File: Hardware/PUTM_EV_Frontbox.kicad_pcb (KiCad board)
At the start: 4 copper layers, 97 x 70 mm, 188 parts, among them IC1 TPS54202HDDCR, J1 XIAO ESP32S3 Sense, J2 Conn_02x16_Counter_Clockwise, J3 FTSH-107-01-L-D-K, Q1 SI2347DS-T1-GE3, U1 TLV743P, U10 MCP6N11-001E/SN, U11 MCP6002-xSN, U12 TLP291-4, U13 TLP291-4, U14 FODM217B, U2 TLV743P, U3 TLV743P, U4 TLV743P, U5 LM4040C33FTA, U6 STM32G484RETx, U7 ADM3057ExRW, U8 ADM3057ExRW, U9 MCP6N11-001E/SN, Y1 ATX-11-F-32.000MHZ-F05-T

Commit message: Sync
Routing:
- net /Connector/DRIVER_KILL: track 103.8 -> 105.6 mm
- net GND: vias 178 -> 183
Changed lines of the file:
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@@
 	)
 	(via
+		(at 144.8 111.4)
+		(size 0.56)
+		(drill 0.3)
+		(layers "F.Cu" "B.Cu")
+		(free yes)
+		(net 2)
+	)
+	(via
 		(at 67.2 99.4)
 		(size 0.56)
@@
 	)
 	(via
+		(at 144.8 112.2)
+		(size 0.56)
+		(drill 0.3)
+		(layers "F.Cu" "B.Cu")
+		(free yes)
+		(net 2)
+	)
+	(via
 		(at 140.5 146)
 		(size 0.56)
@@
 	)
 	(via
+		(at 144 112.2)
+		(size 0.56)
+		(drill 0.3)
+		(layers "F.Cu" "B.Cu")
+		(free yes)
+		(net 2)
+	)
+	(via
 		(at 131 146)
 		(size 0.56)
@@
 	)
 	(via
+		(at 143 111.6)
+		(size 0.56)
+		(drill 0.3)
+		(layers "F.Cu" "B.Cu")
+		(free yes)
+		(net 2)
+	)
+	(via
 		(at 99.2 108.6)
 		(size 0.56)
@@
 	)
 	(via
+		(at 144 111.4)
+		(size 0.56)
+		(drill 0.3)
+		(layers "F.Cu" "B.Cu")
+		(free yes)
+		(net 2)
+	)
+	(via
 		(at 128.5 146)
 		(size 0.56)
@@
 	)
 	(via
-		(at 110.683652 106.613332)
+		(at 111.98 107.06)
 		(size 0.56)
 		(drill 0.3)
@@
 	)
 	(segment
-		(start 110.683652 106.613332)
-		(end 111.13032 107.06)
+		(start 111.98 107.06)
+		(end 133.35 107.06)
 		(width 0.4)
 		(layer "B.Cu")
@@
 	)
 	(segment
-		(start 111.13032 107.06)
-		(end 133.35 107.06)
+		(start 104.338232 92.351)
+		(end 111.261768 92.351)
 		(width 0.4)
-		(layer "B.Cu")
+		(layer "In2.Cu")
 		(net 83)
 	)
 	(segment
-		(start 114.82 89.77)
-		(end 112.239 92.351)
+		(start 99.973 96.716232)
+		(end 99.973 96.413464)
 		(width 0.4)
 		(layer "In2.Cu")
@@
 	)
 	(segment
-		(start 103.579 92.351)
-		(end 99.973 95.957)
+		(start 102.987696 108.38)
+		(end 99.973 105.365304)
 		(width 0.4)
 		(layer "In2.Cu")
@@
 	)
 	(segment
-		(start 114.82 88.3)
-		(end 114.82 89.77)
+		(start 100.295768 95.634232)
+		(end 103.256232 92.673768)
+		(width 0.4)
+		(layer "In2.Cu")
+		(net 83)
+	)
+	(segment
+		(start 104.035464 92.351)
+		(end 104.338232 92.351)
+		(width 0.4)
+		(layer "In2.Cu")
+		(net 83)
+	)
+	(segment
+		(start 99.973 95.957)
+		(end 100.295768 95.634232)
+		(width 0.4)
+		(layer "In2.Cu")
+		(net 83)
+	)
+	(segment
+		(start 103.256232 92.673768)
+		(end 103.579 92.351)
 		(width 0.4)
 		(layer "In2.Cu")
@@
 	(segment
 		(start 115.32 87.8)
-		(end 114.82 88.3)
+		(end 119.96 87.8)
 		(width 0.4)
 		(layer "In2.Cu")
@@
 	)
 	(segment
-		(start 99.973 95.957)
-		(end 99.973 104.253)
+		(start 103.881768 92.351)
+		(end 104.035464 92.351)
 		(width 0.4)
 		(layer "In2.Cu")
@@
 	)
 	(segment
-		(start 99.973 104.253)
-		(end 102.333332 106.613332)
+		(start 110.66 108.38)
+		(end 102.987696 108.38)
 		(width 0.4)
 		(layer "In2.Cu")
@@
 	)
 	(segment
-		(start 102.333332 106.613332)
-		(end 110.683652 106.613332)
+		(start 99.973 105.365304)
+		(end 99.973 104.709464)
 		(width 0.4)
 		(layer "In2.Cu")
@@
 	)
 	(segment
-		(start 121.16 89)
-		(end 119.96 87.8)
+		(start 133.35 107.06)
+		(end 133.687208 107.06)
 		(width 0.4)
 		(layer "In2.Cu")
@@
 	)
 	(segment
-		(start 133.35 107.06)
-		(end 133.687208 107.06)
+		(start 119.96 87.8)
+		(end 121.16 89)
+		(width 0.4)
+		(layer "In2.Cu")
+		(net 83)
+	)
+	(segment
+		(start 99.973 96.413464)
+		(end 99.973 96.259768)
+		(width 0.4)
+		(layer "In2.Cu")
+		(net 83)
+	)
+	(segment
+		(start 111.718232 92.351)
+		(end 112.239 92.351)
 		(width 0.4)
 		(layer "In2.Cu")
@@
 	(segment
 		(start 112.239 92.351)
-		(end 103.579 92.351)
+		(end 114.82 89.77)
 		(width 0.4)
 		(layer "In2.Cu")
@@
 	)
 	(segment
-		(start 119.96 87.8)
+		(start 99.973 104.253)
+		(end 99.973 103.796536)
+		(width 0.4)
+		(layer "In2.Cu")
+		(net 83)
+	)
+	(segment
+		(start 99.973 103.796536)
+		(end 99.973 96.716232)
+		(width 0.4)
+		(layer "In2.Cu")
+		(net 83)
+	)
+	(segment
+		(start 99.973 96.259768)
+		(end 99.973 95.957)
+		(width 0.4)
+		(layer "In2.Cu")
+		(net 83)
+	)
+	(segment
+		(start 111.98 107.06)
+		(end 110.66 108.38)
+		(width 0.4)
+		(layer "In2.Cu")
+		(net 83)
+	)
+	(segment
+		(start 114.82 89.77)
+		(end 114.82 88.3)
+		(width 0.4)
+		(layer "In2.Cu")
+		(net 83)
+	)
+	(segment
+		(start 111.261768 92.351)
+		(end 111.718232 92.351)
+		(width 0.4)
+		(layer "In2.Cu")
+		(net 83)
+	)
+	(segment
+		(start 99.973 104.709464)
+		(end 99.973 104.253)
+		(width 0.4)
+		(layer "In2.Cu")
+		(net 83)
+	)
+	(segment
+		(start 114.82 88.3)
 		(end 115.32 87.8)
 		(width 0.4)
@@
 	)
 	(segment
+		(start 103.579 92.351)
+		(end 103.881768 92.351)
+		(width 0.4)
+		(layer "In2.Cu")
+		(net 83)
+	)
+	(segment
 		(start 142.8 123.707631)
 		(end 143.169 123.338631)
@@
 			)
 		)
+	)
+	(zone
+		(net 0)
+		(net_name "")
+		(layers "F.Cu" "In1.Cu" "In2.Cu")
+		(hatch edge 0.5)
+		(connect_pads
+			(clearance 0)
+		)
+		(min_thickness 0.25)
+		(filled_areas_thickness no)
+		(keepout
+			(tracks allowed)
+			(vias allowed)
+			(pads allowed)
+			(copperpour not_allowed)
+			(footprints allowed)
+		)
+		(placement
+			(enabled no)
+			(sheetname "")
+		)
+		(fill
+			(thermal_gap 0.5)
+			(thermal_bridge_width 0.5)
+		)
+		(polygon
+			(pts
+				(xy 145.2 110.4) (xy 151.2 110.4) (xy 151.2 113.6) (xy 145.2 113.6)
+			)
+		)

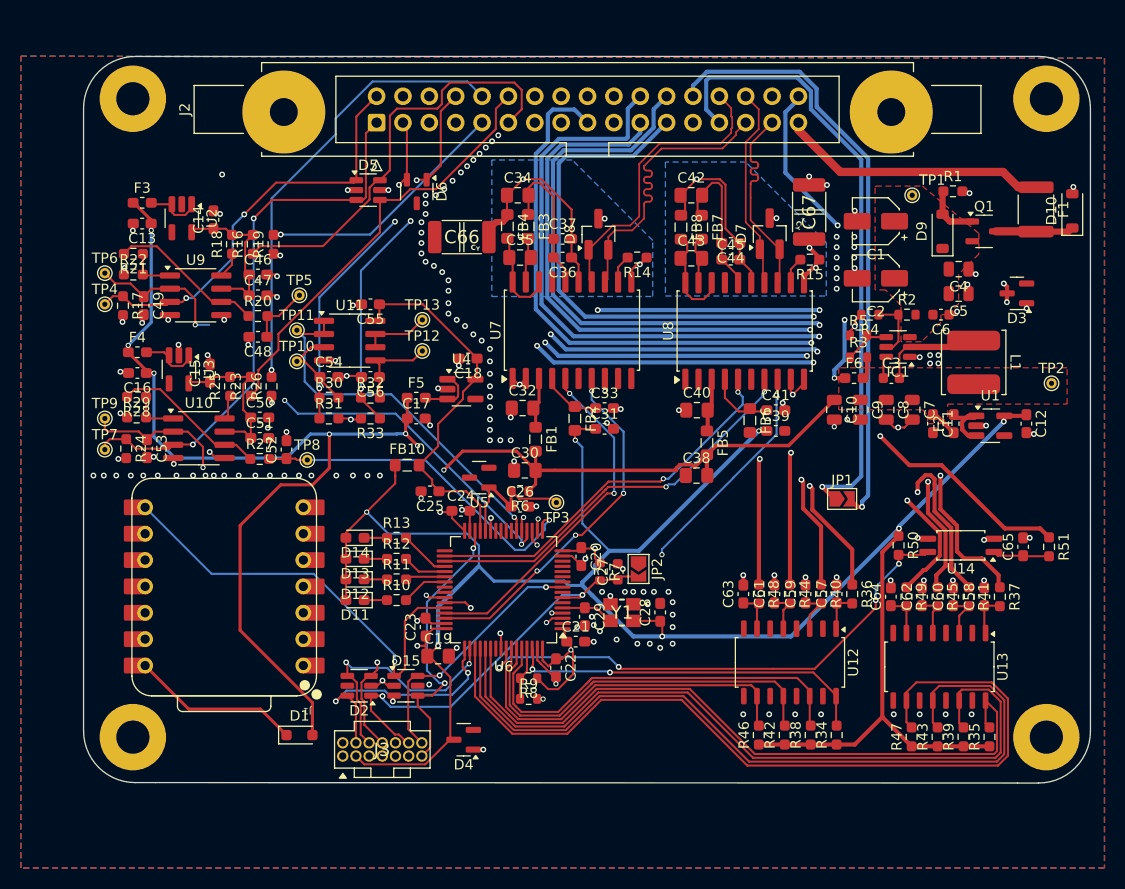
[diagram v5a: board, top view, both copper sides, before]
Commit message: Changed safety sensing routing
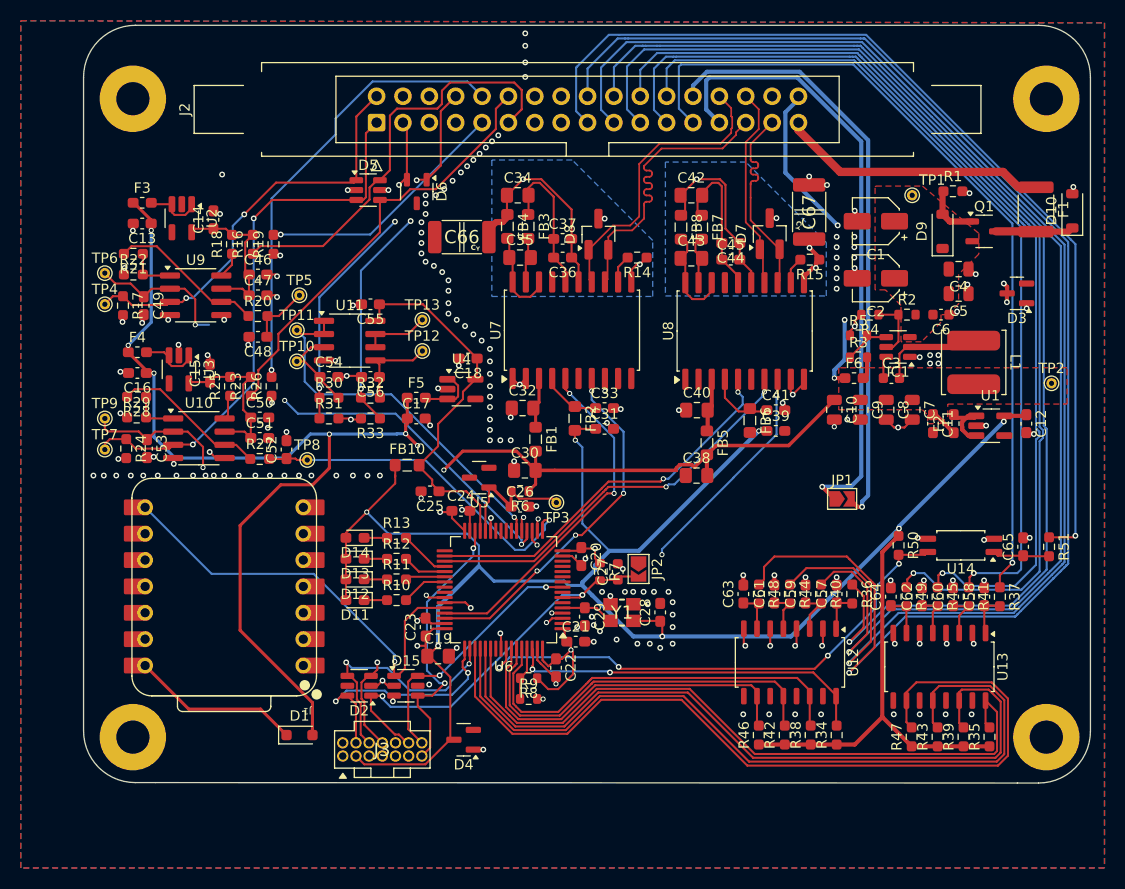
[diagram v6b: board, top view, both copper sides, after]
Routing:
- net /Connector/RIGHT_WHEEL: track 88.9 -> 138.3 mm, vias 3 -> 1
- net /Connector/OVERTRAVEL: track 87.6 -> 132.5 mm, vias 3 -> 1
- net /Connector/BSPD: track 84.7 -> 115.0 mm, vias 2 -> 1
- net /Connector/RIGHT_KILL: track 94.6 -> 121.6 mm, vias 3 -> 1
- net /Connector/DRIVER_KILL: track 105.6 -> 80.1 mm, vias 3 -> 1
- net /Connector/EBS: track 82.0 -> 94.1 mm, vias 2 -> 1
- net GND: track 77.8 -> 88.8 mm, vias 183 -> 195
- net /Connector/INERTIA: track 86.3 -> 96.8 mm, vias 2 -> 1
- net /Connector/LEFT_WHEEL: track 84.1 -> 94.2 mm, vias 2 -> 1
- net /Connector/LEFT_KILL: track 89.2 -> 83.0 mm, vias 2 -> 1
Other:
- board size 97 x 70 mm -> 97 x 73 mm

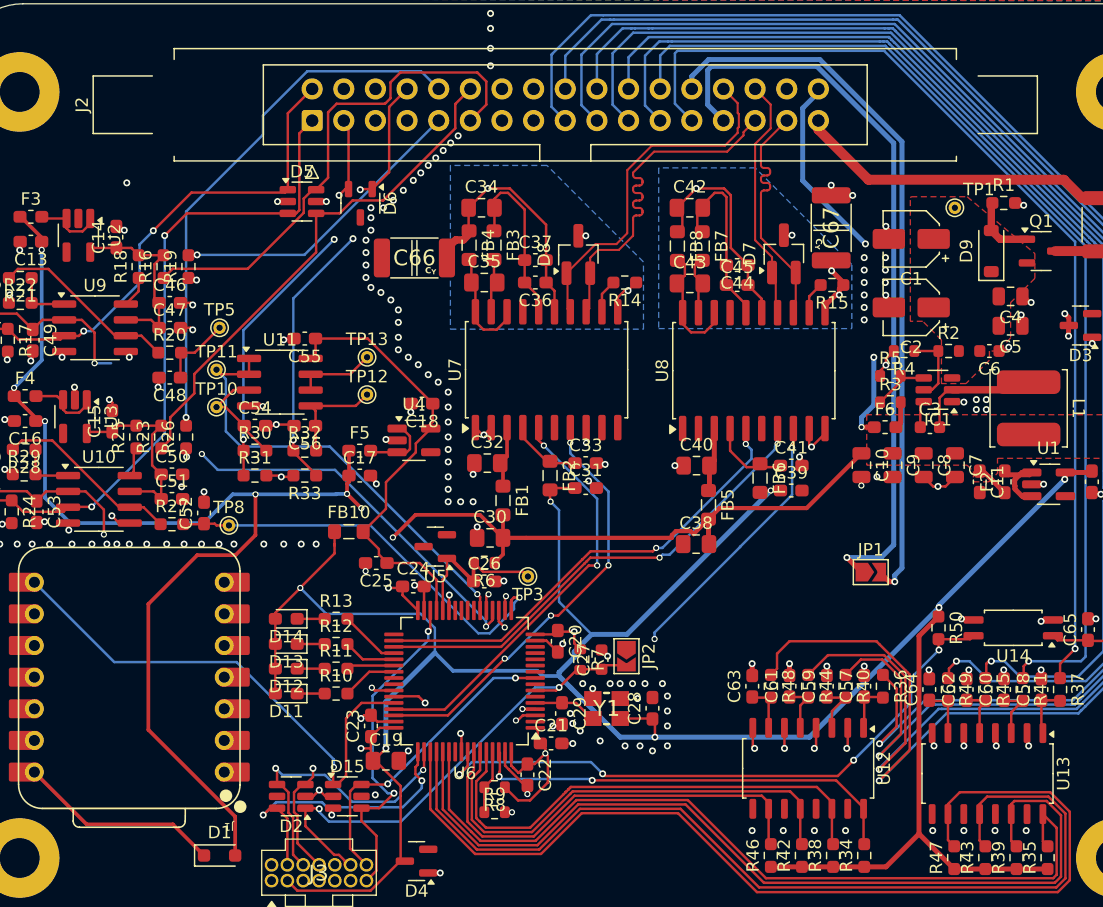
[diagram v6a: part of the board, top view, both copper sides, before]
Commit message: Added better grounding and clearance between GND and CAN_ISO_GND
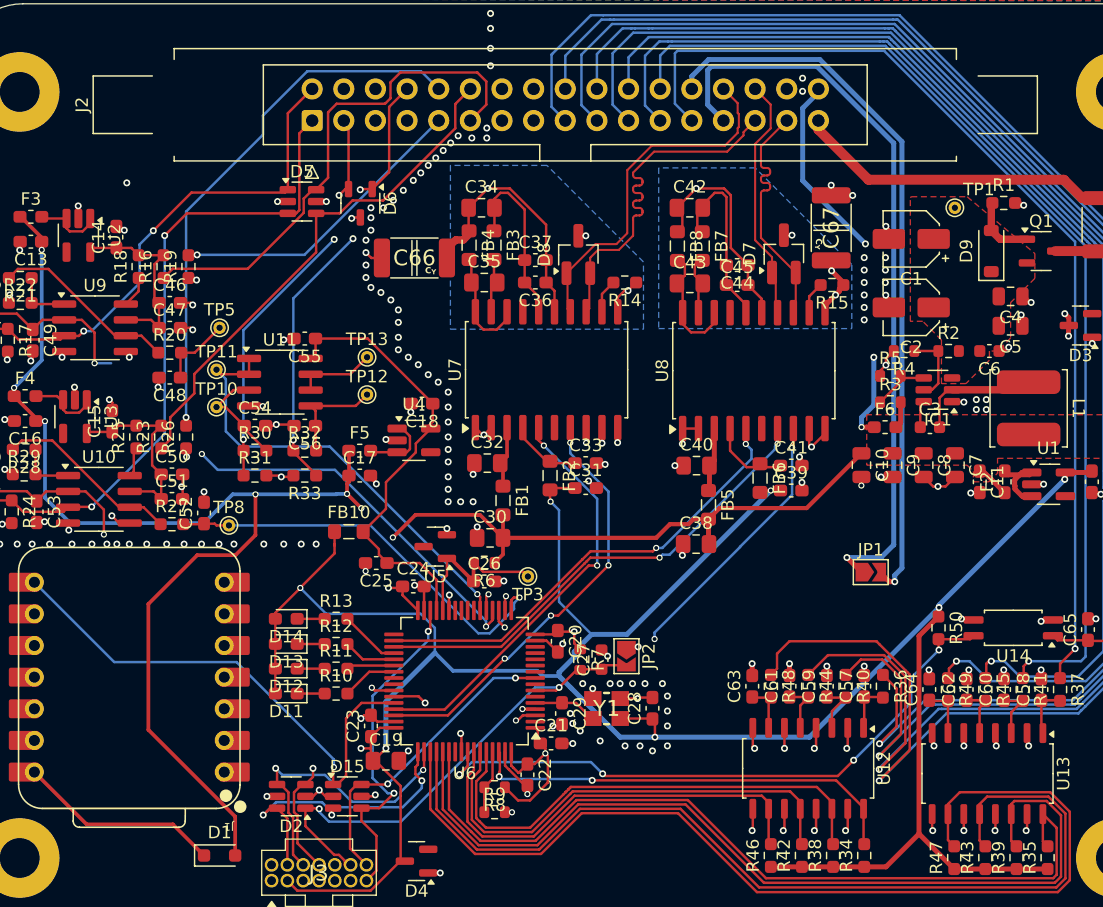
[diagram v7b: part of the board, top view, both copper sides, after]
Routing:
- net GND: track 88.8 -> 121.8 mm, vias 195 -> 211
